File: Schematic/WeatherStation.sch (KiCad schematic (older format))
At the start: 67 parts, among them J1 SolarPanels, J2 TowerPlug, J3 Battery, J4 Battery, J5 BME Connector, J6 Lux Connector, J7 BME Connector, Q1 FQP30N06L, Q2 FQP27P06, Q3 FQP27P06, Q4 FQP30N06L, Q5 FQP27P06, SW1 SW_RESET, U1 MCP1826-ADJ, U2 TC4056A_BASED_CHARGER, U3 ATmega328P-PU, U4 BME280Breakout, U5 23LC1024, U6 NodeMCU_1.0_(ESP-12E), U7 MCP23008, U8 RTCModule, Y1 16MHz

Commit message: Schematic Updates
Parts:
- removed C4: 1uF, Capacitors_THT:CP_Radial_D5.0mm_P2.50mm, symbol CP_Small
- removed C6: 100pF, symbol C_Small
- removed J3, J4: Battery, symbol Conn_01x02
- added J10, J9: ESP Connector, Connectors_JST:JST_XH_B06B-XH-A_06x2.50mm_Straight, symbol Conn_01x06
- added J11: Conn_01x02, Connectors_JST:JST_XH_B02B-XH-A_02x2.50mm_Straight, symbol Conn_01x02
- added J3: ICSP Header, Pin_Headers:Pin_Header_Straight_1x04_Pitch2.54mm, symbol Conn_01x04
- added J4: Conn_01x05, Connectors_JST:JST_XH_B07B-XH-A_07x2.50mm_Straight, symbol Conn_01x07
- added J8: Conn_01x05, Connectors_JST:JST_XH_B05B-XH-A_05x2.50mm_Straight, symbol Conn_01x05
- added JP1: Jumper, Pin_Headers:Pin_Header_Straight_1x02_Pitch2.54mm, symbol Jumper
- added Q6: FQP30N06L, TO_SOT_Packages_THT:TO-220-3_Vertical, symbol FQP30N06L
- added Q7: FQP27P06, TO_SOT_Packages_THT:TO-220-3_Vertical, symbol FQP27P06
- added R20: 10K, Resistors_THT:R_Axial_DIN0207_L6.3mm_D2.5mm_P7.62mm_Horizontal, symbol R
- added R21: 100k, Resistors_THT:R_Axial_DIN0207_L6.3mm_D2.5mm_P7.62mm_Horizontal, symbol R
- added R22: 10K, symbol R
- C1: footprint Capacitors_THT:C_Disc_D4.3mm_W1.9mm_P5.00mm -> Capacitors_THT:C_Disc_D5.0mm_W2.5mm_P5.00mm
- C10, C11, C15, C16, C17, C18, C20, C3, C5, C8: footprint (none) -> Capacitors_THT:C_Disc_D5.0mm_W2.5mm_P5.00mm
- C12, C7: footprint (none) -> Capacitors_THT:CP_Radial_D5.0mm_P2.50mm
- C13, C14: footprint (none) -> Capacitors_THT:CP_Radial_D8.0mm_P2.50mm
- C19: footprint (none) -> Capacitors_THT:CP_Radial_D4.0mm_P2.00mm
- C2: footprint (none) -> Capacitors_THT:C_Disc_D5.1mm_W3.2mm_P5.00mm
- C9: footprint (none) -> Capacitors_THT:CP_Radial_D6.3mm_P2.50mm
- D1, D2: footprint Diodes_THT:D_DO-41_SOD81_P7.62mm_Horizontal -> Diodes_THT:D_DO-15_P12.70mm_Horizontal
- D3: symbol TL1431AIZT -> TL1431AIZT-RESCUE-WeatherStation
- D4, D5: footprint (none) -> LEDs:LED_D5.0mm
- J5, J6, J7: footprint (none) -> Connectors_JST:JST_XH_B04B-XH-A_04x2.50mm_Straight
- R1, R10, R11, R12, R13, R14, R15, R16, R17, R18, R19, R2, R5: footprint (none) -> Resistors_THT:R_Axial_DIN0207_L6.3mm_D2.5mm_P7.62mm_Horizontal
- R4: value 12K -> 10K; footprint (none) -> Resistors_THT:R_Axial_DIN0207_L6.3mm_D2.5mm_P7.62mm_Horizontal
- R7: value 82K -> 100K; footprint (none) -> Resistors_THT:R_Axial_DIN0207_L6.3mm_D2.5mm_P7.62mm_Horizontal
- R8: value 112k -> 100k; footprint Resistors_THT:R_Axial_DIN0207_L6.3mm_D2.5mm_P7.62mm_Horizontal -> Resistors_THT:R_Axial_DIN0204_L3.6mm_D1.6mm_P7.62mm_Horizontal
- R9: value 110 -> 1.1K; footprint (none) -> Resistors_THT:R_Axial_DIN0207_L6.3mm_D2.5mm_P7.62mm_Horizontal
- SW1: footprint (none) -> Buttons_Switches_THT:SW_PUSH_6mm
- U2: footprint (none) -> WeatherLibrary:TC4056_BREAKOUT
- U3: footprint Package_DIP:DIP-28_W7.62mm -> Housings_DIP:DIP-28_W7.62mm_Socket
- U5: footprint (none) -> Housings_DIP:DIP-8_W7.62mm_Socket
- U6: footprint ESP8266:NodeMCU1.0(12-E) -> WeatherLibrary:ESP8266_NODEMCU
- Y1: footprint (none) -> Crystals:Crystal_HC52-8mm_Vertical
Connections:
- net labels added: Bat+, Bat-, BatV+, BatV-, ESP_Enable, RainBucket, Reset, SCL, SDA, SRAM_CS, SerialRX, SerialTX
- net labels removed: +BATT, -BATT
- wire segments 214 -> 265
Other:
- note added: "VCC Reading?"
- note removed: "RainBucket"
- note removed: "SerialTX"
- moved on the sheet: BT1, C1, C12, C13, C14, C15, C16, C17, C2, C3, C5, C7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

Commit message: C : : Updated Schemati
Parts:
- removed C1: 100nF, Capacitors_THT:C_Disc_D5.0mm_W2.5mm_P5.00mm, symbol C
- added C1, C4: 10uF, Capacitors_THT:CP_Radial_D5.0mm_P2.50mm, symbol C_Small
- added J12: Rain_Conn, Connectors_JST:JST_XH_B02B-XH-A_02x2.50mm_Straight, symbol Conn_01x02
- added L1: 10uF, Inductors_THT:L_Axial_L5.3mm_D2.2mm_P7.62mm_Horizontal_Vishay_IM-1, symbol INDUCTOR
- added R23: 1k, Resistors_THT:R_Axial_DIN0207_L6.3mm_D2.5mm_P7.62mm_Horizontal, symbol R
- added R24: 10K, Resistors_THT:R_Axial_DIN0207_L6.3mm_D2.5mm_P7.62mm_Horizontal, symbol R
- J3, J6: symbol Conn_01x04 -> Conn_01x05
- J9: footprint Connectors_JST:JST_XH_B06B-XH-A_06x2.50mm_Straight -> Connectors_JST:JST_XH_B06B-XH-A_07x2.50mm_Straight; symbol Conn_01x06 -> Conn_01x07
- R22: footprint (none) -> Resistors_THT:R_Axial_DIN0207_L6.3mm_D2.5mm_P7.62mm_Horizontal
- R6: value 4.7k -> 1k
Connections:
- net Anemometer: now also R3.2, C4.2; no longer R3.1
- net DivBatV: now also J4.6 (Pin_6), U3.23 (PC0); no longer J4.7 (Pin_7), U3.25 (PC2)
- net EspRX: now also J9.1 (Pin_1); no longer J9.2 (Pin_2)
- net EspReset: now also J9.6 (Pin_6), U7.15 (GP5); no longer J9.4 (Pin_4), U3.6 (PD4)
- net EspResult: now also J9.5 (Pin_5), U7.16 (GP6); no longer J9.1 (Pin_1), U3.13 (PD7)
- net EspSuccess: now also J9.4 (Pin_4), U7.17 (GP7); no longer U7.16 (GP6)
- net EspTX: now also J9.2 (Pin_2); no longer J9.3 (Pin_3)
- net GND: now also C10.1, C11.2, D3.2 (A), J2.2 (Pin_2), J3.5 (Pin_5), J4.7 (Pin_7), J9.3 (Pin_3), R3.1, C1.2, C4.1, R24.1; no longer C10.2, C11.1, D3.3 (K), J2.1 (Pin_1), J4.5 (Pin_5), J9.6 (Pin_6), R3.2
- net RainBucket: now also C1.1, R23.1, R24.2
- net RefV: now also D3.3 (K), J4.5 (Pin_5), U3.24 (PC1); no longer D3.2 (A), J4.6 (Pin_6), U3.26 (PC3)
- net VCC: now also C10.2, J10.5 (Pin_5), J2.1 (Pin_1), J9.7 (Pin_7), J12.2 (Pin_2), L1.2; no longer C10.1, C11.2, J2.2 (Pin_2), J9.5 (Pin_5), U3.20 (AVCC)
- net WindVane: now also U3.26 (PC3); no longer U3.24 (PC1)
- net XTAL2: now reaches C16.2, U3.10 (XTAL2/PB7), Y1.2
- net OK_LED: now reaches R14.1, U3.14 (PB0)
- net ERROR_LED: now reaches R15.1, U3.15 (PB1)
- net MOSI: now reaches J3.3 (Pin_3), U3.17 (PB3/MOSI), U5.5 (SI/SIO0)
- net MISO: now reaches J3.2 (Pin_2), U3.18 (PB4/MISO), U5.2 (SO/SIO1)
- net SCK: now reaches J3.1 (Pin_1), U3.19 (PB5/SCK), U5.6 (SCK)
- net AREF: now reaches C8.1, U3.21 (AREF)
- net XTAL1: now reaches C15.2, U3.9 (XTAL1/PB6), Y1.1
- net at C12.1, C13.1, C14.1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: no longer J10.5 (Pin_5)
- net ESP_Enable renamed ESP_ENABLE
- new net: J12.1 (Pin_1), R23.2
- new net AVCC: C11.1, L1.1, U3.20 (AVCC)
- no-connect marks 35 -> 36
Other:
- note removed: "VCC Reading?"
- moved on the sheet: C10, C11, C9, J2, J4, R3, R6

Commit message: This
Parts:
- removed J10: ESP Connector, Connectors_JST:JST_XH_B06B-XH-A_06x2.50mm_Straight, symbol Conn_01x06
- removed Q6: FQP30N06L, TO_SOT_Packages_THT:TO-220-3_Vertical, symbol FQP30N06L
- removed Q7: FQP27P06, TO_SOT_Packages_THT:TO-220-3_Vertical, symbol FQP27P06
- added C6: 100nF, Capacitors_THT:C_Disc_D5.0mm_W2.5mm_P5.00mm, symbol C_Small
- added J10: ESP Connector, Connectors_JST:JST_XH_B06B-XH-A_07x2.50mm_Straight, symbol Conn_01x07
- added J13: Serial, Pin_Headers:Pin_Header_Straight_1x02_Pitch2.54mm, symbol Conn_01x02
- added J14: Board_Power_B, Connectors_JST:JST_XH_B03B-XH-A_03x2.50mm_Straight, symbol Conn_01x03
- added JP2: Jumper, Pin_Headers:Pin_Header_Straight_1x02_Pitch2.54mm, symbol Jumper
- added R25: 4.7k, Resistors_THT:R_Axial_DIN0207_L6.3mm_D2.5mm_P7.62mm_Horizontal, symbol R
- C1, C4: value 10uF -> 330nF
- J11: value Conn_01x02 -> PSU_Conn_B
- J3: value ICSP Header -> AVR_PROG_HEADER; footprint Pin_Headers:Pin_Header_Straight_1x04_Pitch2.54mm -> Pin_Headers:Pin_Header_Straight_1x06_Pitch2.54mm; symbol Conn_01x05 -> Conn_01x06
- J4: value Conn_01x05 -> Board_Power_A; footprint Connectors_JST:JST_XH_B07B-XH-A_07x2.50mm_Straight -> WeatherLibrary:JST_XH_B04B-XH-A_04x2.54mm_Straight; symbol Conn_01x07 -> Conn_01x04
- J8: value Conn_01x05 -> PSU_Conn_A
- L1: value 10uF -> 100uH
- R22: value 10K -> 4.7k
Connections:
- net BatDivEnable: now also J14.3 (Pin_3); no longer J4.3 (Pin_3)
- net DivBatV: now also J4.3 (Pin_3); no longer J4.6 (Pin_6)
- net EspRX: now also J9.3 (Pin_3), U6.22 (D6(GPIO12)), J10.5 (Pin_5); no longer J9.1 (Pin_1), U6.23 (D5(GPIO14))
- net EspReset: now also J9.7 (Pin_7), J10.1 (Pin_1); no longer J9.6 (Pin_6)
- net EspResult: now also J9.6 (Pin_6), J10.2 (Pin_2); no longer J9.5 (Pin_5)
- net EspSuccess: now also J9.5 (Pin_5), J10.3 (Pin_3); no longer J9.4 (Pin_4)
- net EspTX: now also U6.23 (D5(GPIO14)), J10.6 (Pin_6); no longer U6.22 (D6(GPIO12))
- net GND: now also J3.6 (Pin_6), J4.4 (Pin_4), J6.5 (Pin_5), J9.1 (Pin_1), U6.17 (GND), U6.24 (GND), U7.9 (VSS), C6.2, J10.7 (Pin_7), JP2.1; no longer D4.1 (K), D5.1 (K), J3.5 (Pin_5), J4.7 (Pin_7), J9.3 (Pin_3), R20.1, U7.18 (VDD)
- net MISO: now also J3.3 (Pin_3); no longer J3.2 (Pin_2)
- net MOSI: now also J3.4 (Pin_4); no longer J3.3 (Pin_3)
- net PanelDisable: now also J14.1 (Pin_1); no longer J4.1 (Pin_1)
- net RefV: now also J4.2 (Pin_2); no longer J4.5 (Pin_5)
- net RefVEnable: now also J14.2 (Pin_2); no longer J4.2 (Pin_2)
- net Reset: now also J3.5 (Pin_5), R16.2, C6.1; no longer J3.4 (Pin_4), R16.1
- net SCK: now also J3.2 (Pin_2); no longer J3.1 (Pin_1)
- net SCL: now also J6.3 (Pin_3), J7.3 (Pin_3), U3.28 (PC5/SCL), U7.1 (SCL), U8.4 (SCL), R25.2; no longer J6.4 (Pin_4), J7.4 (Pin_4), U3.27 (PC4/SDA), U7.2 (SDA), U8.3 (SDA)
- net SDA: now also J6.4 (Pin_4), J7.4 (Pin_4), R22.2, U3.27 (PC4/SDA), U7.2 (SDA), U8.3 (SDA); no longer J6.3 (Pin_3), J7.3 (Pin_3), U3.28 (PC5/SCL), U7.1 (SCL), U8.4 (SCL)
- net SerialRX: now also J13.1 (Pin_1)
- net SerialTX: now also J13.2 (Pin_2)
- net VCC: now also C12.1, C13.1, C14.1, J3.1 (Pin_1), J4.1 (Pin_1), J9.4 (Pin_4), R16.1, R20.1, R22.1, U6.16 (3.3V), U6.25 (3.3V), U7.18 (VDD), J10.4 (Pin_4), R25.1; no longer J4.4 (Pin_4), J9.7 (Pin_7), R16.2, U7.9 (VSS)
- new net LED_GND: D4.1 (K), D5.1 (K), JP2.2
- no-connect marks 36 -> 28
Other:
- note added: "1K resistor and 330nF = 1.65ms/5RC debounce"
- moved on the sheet: C12, C17, C19, C20, R16, R19, R20, SW1, U5

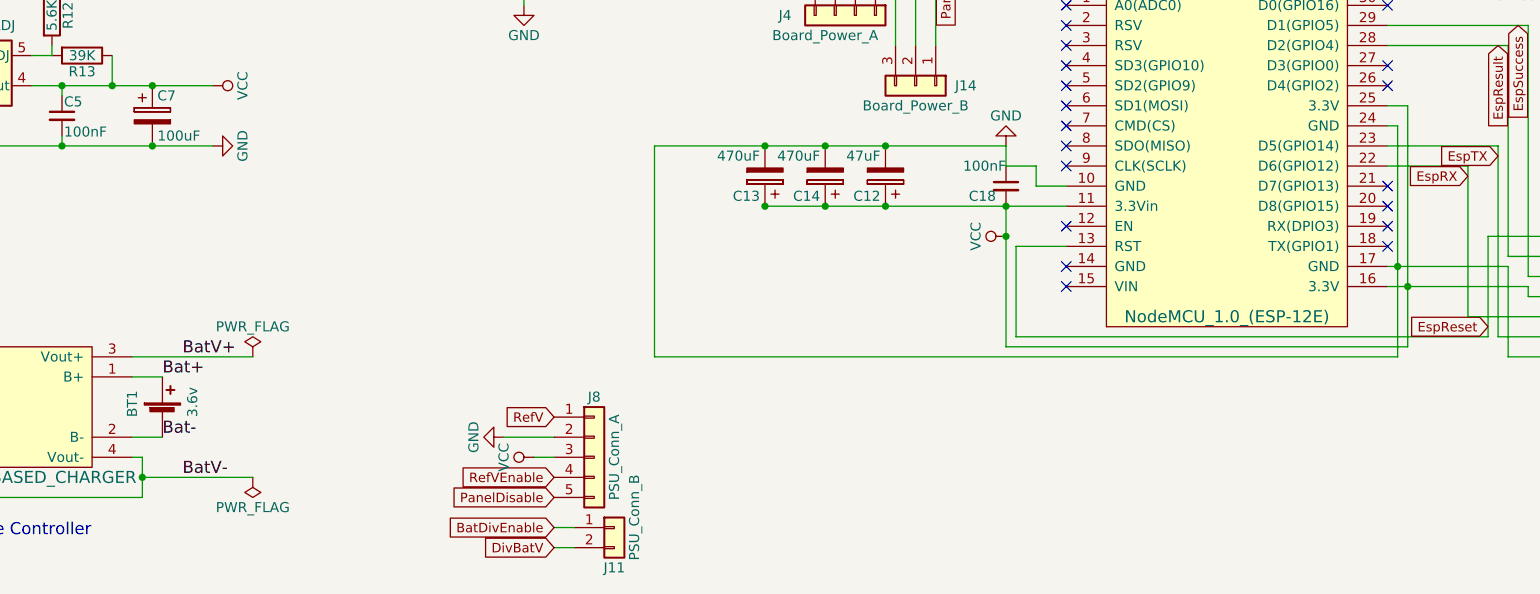
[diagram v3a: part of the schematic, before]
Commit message: Schematic Updates
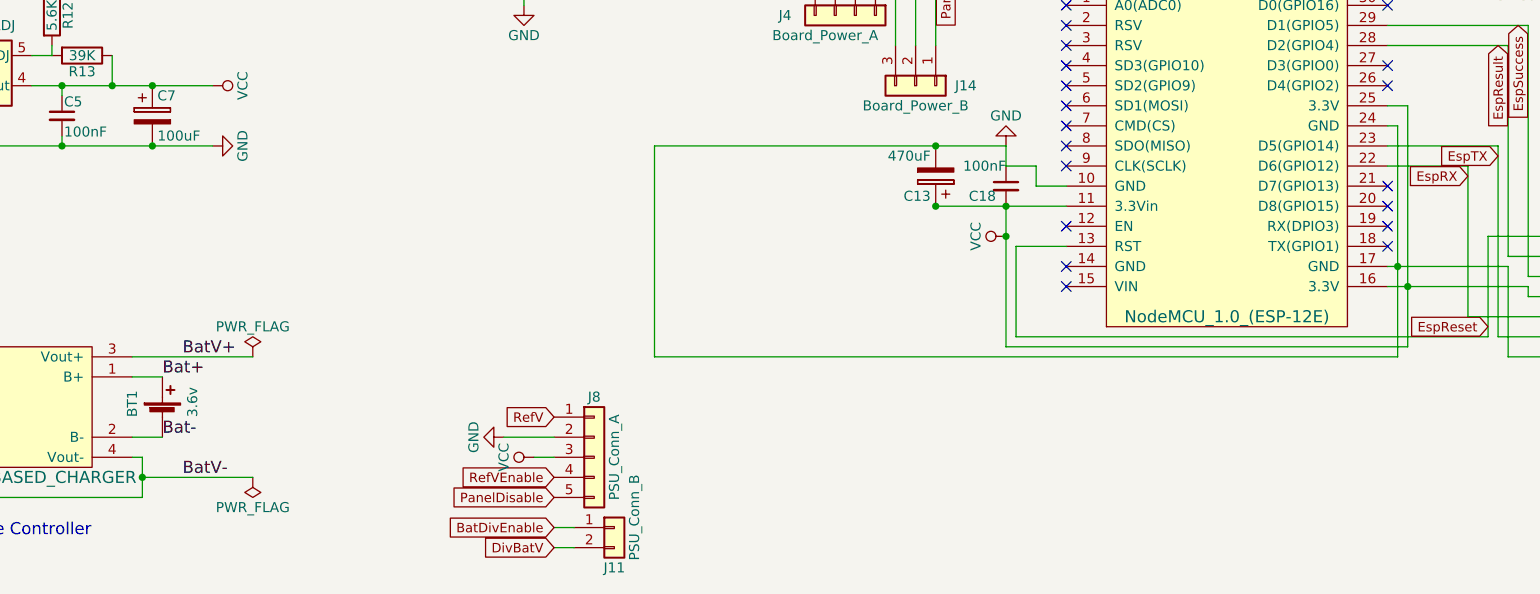
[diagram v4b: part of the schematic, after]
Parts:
- removed C12: 47uF, Capacitors_THT:CP_Radial_D5.0mm_P2.50mm, symbol CP
- removed C14: 470uF, Capacitors_THT:CP_Radial_D8.0mm_P2.50mm, symbol CP
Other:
- moved on the sheet: C13
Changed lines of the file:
@@
-$EndComp
-$Comp
-L CP C14
-U 1 1 5AED1636
-P 7250 5550
-F 0 "C14" H 7275 5650 50  0000 L CNN
-F 1 "470uF" H 7275 5450 50  0000 L CNN
-F 2 "Capacitors_THT:CP_Radial_D8.0mm_P2.50mm" H 7288 5400 50  0001 C CNN
-F 3 "" H 7250 5550 50  0001 C CNN
-	1    7250 5550
-	-1   0    0    1
 $EndComp
 $Comp
 L CP C13
 U 1 1 5AED1A3C
-P 6950 5550
-F 0 "C13" H 6975 5650 50  0000 L CNN
-F 1 "470uF" H 6975 5450 50  0000 L CNN
-F 2 "Capacitors_THT:CP_Radial_D8.0mm_P2.50mm" H 6988 5400 50  0001 C CNN
-F 3 "" H 6950 5550 50  0001 C CNN
-	1    6950 5550
-	-1   0    0    1
-$EndComp
-$Comp
-L CP C12
-U 1 1 5AED1B1F
-P 7550 5550
-F 0 "C12" H 7575 5650 50  0000 L CNN
-F 1 "47uF" H 7575 5450 50  0000 L CNN
-F 2 "Capacitors_THT:CP_Radial_D5.0mm_P2.50mm" H 7588 5400 50  0001 C CNN
-F 3 "" H 7550 5550 50  0001 C CNN
-	1    7550 5550
+P 7800 5550
+F 0 "C13" H 7825 5650 50  0000 L CNN
+F 1 "470uF" H 7825 5450 50  0000 L CNN
+F 2 "Capacitors_THT:CP_Radial_D8.0mm_P2.50mm" H 7838 5400 50  0001 C CNN
+F 3 "" H 7800 5550 50  0001 C CNN
+	1    7800 5550
 	-1   0    0    1
 $EndComp
@@
 Connection ~ 2600 7150
 Wire Wire Line
-	3850 7150 3850 6950
+	3850 6950 3850 7150
 Wire Wire Line
 	3850 7050 4400 7050
@@
 	10750 4800 10050 4800
 Wire Wire Line
-	6950 5700 8450 5700
+	7800 5700 8450 5700
 Connection ~ 8150 5700
-Connection ~ 7250 5700
-Connection ~ 6950 5700
+Connection ~ 7800 5700
 Wire Wire Line
 	6400 5400 8150 5400
-Connection ~ 6950 5400
+Connection ~ 7800 5400
 Wire Wire Line
 	8150 5400 8150 5500
-Connection ~ 7250 5400
 Wire Wire Line
 	8150 5500 8300 5500
@@
 Wire Wire Line
 	8300 5600 8450 5600
-Connection ~ 7550 5700
-Connection ~ 7550 5400
 Connection ~ 3900 5400
 Connection ~ 3900 5100
@@
 	1000 1050 850  1050
 Wire Wire Line
-	6400 6450 10100 6450
+	10100 6450 6400 6450
 Wire Wire Line
 	10150 6400 8150 6400
 Wire Wire Line
-	8150 6400 8150 5700
+	8150 5700 8150 6400
 Connection ~ 8150 5850
 Wire Wire Line
